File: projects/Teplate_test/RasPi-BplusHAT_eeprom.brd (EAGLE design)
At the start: 65 x 56 mm, 1 part, among them X1 RASPI_BOARD_B+_E0

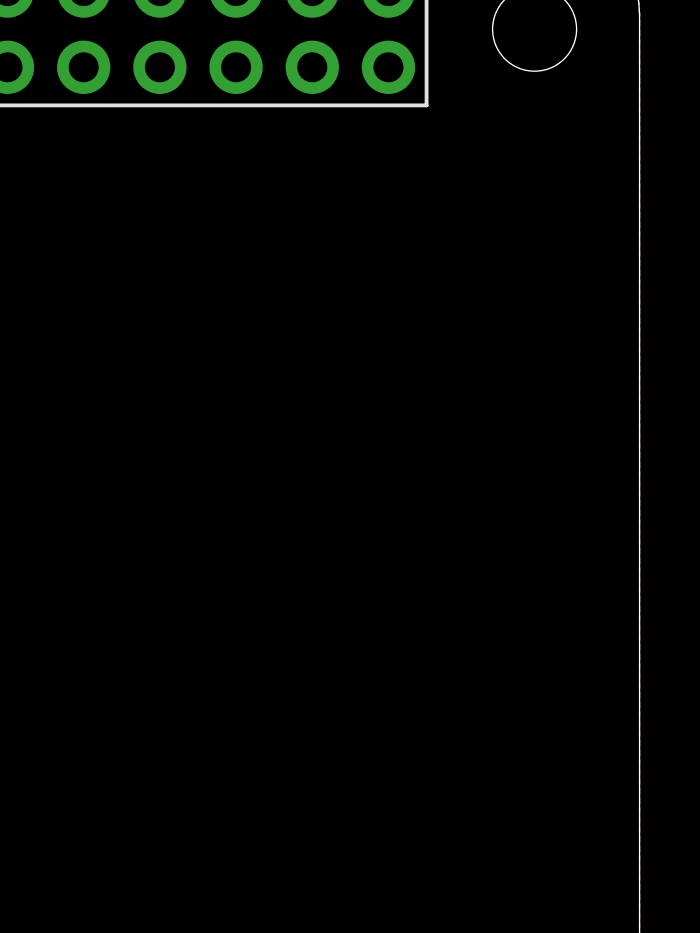
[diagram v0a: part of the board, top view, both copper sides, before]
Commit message: Added an EEPROM version of the template
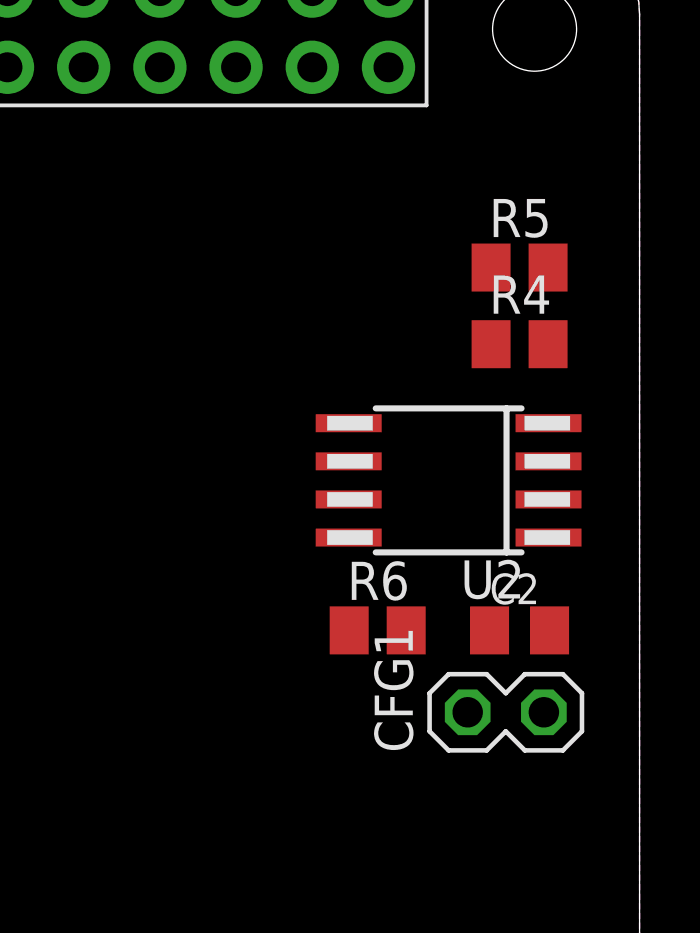
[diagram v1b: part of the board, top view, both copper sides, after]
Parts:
- added C2: 100nF, resistor:C0805K
- added CFG1: (no value), FLYFISH:PIN_W_2
- added R4, R5: 3k9, resistor:M0805
- added R6: 1k, resistor:M0805
- added U2: EEPROM24, FLYFISH:SOIC8
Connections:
- removed net 3V3: X1.1
- removed net 5V0: X1.2
- new net +3V3: C2.1, R4.2, R5.2, R6.2, U2.8, X1.1, X1.17
- new net +5V: X1.2, X1.4
- new net N$4: R4.1, U2.6, X1.28
- new net N$5: R5.1, U2.5, X1.27
- new net N$6: CFG1.1, R6.1, U2.7
- net GND: now also C2.2, CFG1.2, U2.1, U2.2, U2.3, U2.4, X1.14, X1.20, X1.25, X1.30, X1.34, X1.39, X1.9
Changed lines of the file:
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@@
 <layer number="27" name="tValues" color="7" fill="1" visible="no" active="yes"/>
 <layer number="28" name="bValues" color="7" fill="1" visible="no" active="yes"/>
-<layer number="29" name="tStop" color="7" fill="3" visible="no" active="yes"/>
+<layer number="29" name="tStop" color="7" fill="3" visible="yes" active="yes"/>
 <layer number="30" name="bStop" color="7" fill="6" visible="no" active="yes"/>
 <layer number="31" name="tCream" color="7" fill="4" visible="no" active="yes"/>
 <layer number="32" name="bCream" color="7" fill="5" visible="no" active="yes"/>
 <layer number="33" name="tFinish" color="6" fill="3" visible="yes" active="yes"/>
-<layer number="34" name="bFinish" color="6" fill="6" visible="no" active="yes"/>
+<layer number="34" name="bFinish" color="6" fill="6" visible="yes" active="yes"/>
 <layer number="35" name="tGlue" color="7" fill="4" visible="no" active="yes"/>
 <layer number="36" name="bGlue" color="7" fill="5" visible="no" active="yes"/>
@@
 <layer number="97" name="Info" color="7" fill="1" visible="no" active="no"/>
 <layer number="98" name="Guide" color="6" fill="1" visible="no" active="no"/>
+<layer number="100" name="NonViaHole" color="7" fill="1" visible="yes" active="yes"/>
+<layer number="101" name="PlacementGuide" color="7" fill="1" visible="yes" active="yes"/>
+<layer number="102" name="TopSilkscreen" color="7" fill="1" visible="yes" active="yes"/>
+<layer number="103" name="not_populated" color="7" fill="1" visible="yes" active="yes"/>
+<layer number="104" name="BottomSilkscreen" color="7" fill="1" visible="yes" active="yes"/>
+<layer number="105" name="tPlate" color="7" fill="1" visible="yes" active="yes"/>
+<layer number="106" name="bPlate" color="7" fill="1" visible="yes" active="yes"/>
+<layer number="107" name="Crop" color="7" fill="1" visible="yes" active="yes"/>
+<layer number="116" name="Patch_BOT" color="7" fill="1" visible="yes" active="yes"/>
+<layer number="121" name="_tsilk" color="7" fill="1" visible="yes" active="yes"/>
+<layer number="122" name="_bsilk" color="7" fill="1" visible="yes" active="yes"/>
+<layer number="144" name="Drill_legend" color="7" fill="1" visible="yes" active="yes"/>
+<layer number="151" name="HeatSink" color="7" fill="1" visible="yes" active="yes"/>
+<layer number="200" name="200bmp" color="7" fill="1" visible="yes" active="yes"/>
+<layer number="201" name="201bmp" color="7" fill="1" visible="yes" active="yes"/>
+<layer number="202" name="202bmp" color="7" fill="1" visible="yes" active="yes"/>
+<layer number="203" name="203bmp" color="7" fill="1" visible="yes" active="yes"/>
+<layer number="204" name="204bmp" color="7" fill="1" visible="yes" active="yes"/>
+<layer number="205" name="205bmp" color="7" fill="1" visible="yes" active="yes"/>
+<layer number="206" name="206bmp" color="7" fill="1" visible="yes" active="yes"/>
+<layer number="207" name="207bmp" color="7" fill="1" visible="yes" active="yes"/>
+<layer number="208" name="208bmp" color="7" fill="1" visible="yes" active="yes"/>
+<layer number="250" name="Descript" color="7" fill="1" visible="yes" active="yes"/>
+<layer number="251" name="SMDround" color="7" fill="1" visible="yes" active="yes"/>
+<layer number="254" name="cooling" color="7" fill="1" visible="yes" active="yes"/>
 </layers>
 <board>
@@
 <elements>
 <element name="X1" library="raspberrypi_bastelstube_v13" package="RASPI_BOARD_B+_EDGES_0DRILL" value="RASPI_BOARD_B+_E0" x="0" y="0" smashed="yes"/>
+<element name="U2" library="FLYFISH" package="SOIC8" value="EEPROM24" x="58.635" y="37.46" smashed="yes" rot="R90">
+<attribute name="NAME" x="61.175" y="34.793" size="1.27" layer="25" rot="R180"/>
+<attribute name="VALUE" x="61.175" y="41.397" size="1.27" layer="27" rot="R180"/>
+</element>
+<element name="R4" library="resistor" package="M0805" value="3k9" x="61" y="42" smashed="yes">
+<attribute name="NAME" x="59.984" y="43.016" size="1.27" layer="25"/>
+<attribute name="TOLERANCE" value="5%" x="52" y="55" size="1.778" layer="27" display="off"/>
+<attribute name="VALUE" x="59.984" y="39.714" size="1.27" layer="27"/>
+</element>
+<element name="C2" library="resistor" package="C0805K" value="100nF" x="61" y="32.46" smashed="yes">
+<attribute name="DIELECTRIC" value="X7R" x="52" y="45.46" size="1.778" layer="27" display="off"/>
+<attribute name="NAME" x="60" y="33.335" size="1.016" layer="25"/>
+<attribute name="VALUE" x="60" y="30.56" size="1.016" layer="27"/>
+</element>
+<element name="R5" library="resistor" package="M0805" value="3k9" x="61" y="44.555" smashed="yes">
+<attribute name="NAME" x="59.984" y="45.571" size="1.27" layer="25"/>
+<attribute name="TOLERANCE" value="5%" x="47" y="45.555" size="1.778" layer="27" display="off"/>
+<attribute name="VALUE" x="59.984" y="42.269" size="1.27" layer="27"/>
+</element>
+<element name="R6" library="resistor" package="M0805" value="1k" x="56.27" y="32.46" smashed="yes">
+<attribute name="NAME" x="55.254" y="33.476" size="1.27" layer="25"/>
+<attribute name="TOLERANCE" value="5%" x="37.27" y="27.46" size="1.778" layer="27" display="off"/>
+<attribute name="VALUE" x="55.254" y="30.174" size="1.27" layer="27"/>
+</element>
+<element name="CFG1" library="FLYFISH" package="PIN_W_2" value="" x="59.27" y="29.73" smashed="yes" rot="R90">
+<attribute name="NAME" x="57.4412" y="28.3838" size="1.27" layer="25" ratio="10" rot="R90"/>
+<attribute name="VALUE" x="64.985" y="28.46" size="1.27" layer="27" rot="R90"/>
+</element>
 </elements>
 <signals>
@@
 </polygon>
 <contactref element="X1" pad="6"/>
-</signal>
-<signal name="5V0">
+<contactref element="X1" pad="20"/>
+<contactref element="X1" pad="14"/>
+<contactref element="X1" pad="25"/>
+<contactref element="X1" pad="30"/>
+<contactref element="X1" pad="34"/>
+<contactref element="X1" pad="39"/>
+<contactref element="X1" pad="9"/>
+<contactref element="U2" pad="4"/>
+<contactref element="U2" pad="3"/>
+<contactref element="U2" pad="1"/>
+<contactref element="U2" pad="2"/>
+<contactref element="CFG1" pad="2"/>
+<contactref element="C2" pad="2"/>
+</signal>
+<signal name="+3V3">
+<contactref element="X1" pad="1"/>
+<contactref element="X1" pad="17"/>
+<contactref element="U2" pad="8"/>
+<contactref element="R5" pad="2"/>
+<contactref element="R4" pad="2"/>
+<contactref element="R6" pad="2"/>
+<contactref element="C2" pad="1"/>
+<wire x1="61.95" y1="42" x2="61.95" y2="44.555" width="0" layer="19" extent="1-1"/>
+<wire x1="55.305" y1="35.555" x2="61.95" y2="42" width="0" layer="19" extent="1-1"/>
+<wire x1="57.22" y1="32.46" x2="55.305" y2="35.555" width="0" layer="19" extent="1-1"/>
+<wire x1="60" y1="32.46" x2="57.22" y2="32.46" width="0" layer="19" extent="1-1"/>
+<wire x1="28.69" y1="51.23" x2="55.305" y2="35.555" width="0" layer="19" extent="1-1"/>
+<wire x1="8.37" y1="51.23" x2="28.69" y2="51.23" width="0" layer="19" extent="1-1"/>
+</signal>
+<signal name="+5V">
 <contactref element="X1" pad="2"/>
-</signal>
-<signal name="3V3">
-<contactref element="X1" pad="1"/>
+<contactref element="X1" pad="4"/>
+<wire x1="8.37" y1="53.77" x2="10.91" y2="53.77" width="0" layer="19" extent="1-1"/>
+</signal>
+<signal name="N$4">
+<contactref element="U2" pad="6"/>
+<contactref element="R4" pad="1"/>
+<contactref element="X1" pad="28"/>
+<wire x1="55.305" y1="38.095" x2="60.05" y2="42" width="0" layer="19" extent="1-1"/>
+<wire x1="41.39" y1="53.77" x2="55.305" y2="38.095" width="0" layer="19" extent="1-1"/>
+</signal>
+<signal name="N$5">
+<contactref element="U2" pad="5"/>
+<contactref element="R5" pad="1"/>
+<contactref element="X1" pad="27"/>
+<wire x1="55.305" y1="39.365" x2="60.05" y2="44.555" width="0" layer="19" extent="1-1"/>
+<wire x1="41.39" y1="51.23" x2="55.305" y2="39.365" width="0" layer="19" extent="1-1"/>
+</signal>
+<signal name="N$6">
+<contactref element="U2" pad="7"/>
+<contactref element="R6" pad="1"/>
+<contactref element="CFG1" pad="1"/>
+<wire x1="55.32" y1="32.46" x2="55.305" y2="36.825" width="0" layer="19" extent="1-1"/>
+<wire x1="59.27" y1="29.73" x2="55.32" y2="32.46" width="0" layer="19" extent="1-1"/>
 </signal>
 </signals>
